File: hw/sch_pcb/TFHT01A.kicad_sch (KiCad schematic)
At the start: 13 parts, among them J2 SM04B-GHS-TB, M2 M3, U3 MIC5504-3.3YM5

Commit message: Update schematics title block.
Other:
- title: TFI2CEXT01A -> TFHT01A
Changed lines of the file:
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@@
   (paper "A4")
   (title_block
-    (title "TFI2CEXT01A")
-    (date "2021-01-23")
+    (title "TFHT01A")
+    (date "2021-04-05")
     (company "ThunderFly s.r.o.")
-    (comment 1 "I2C expander")
+    (comment 1 "Humidity and Temperature \\n sensor \\n ")
     (comment 2 "Jacho  <info@thunderfly.cz>")
   )

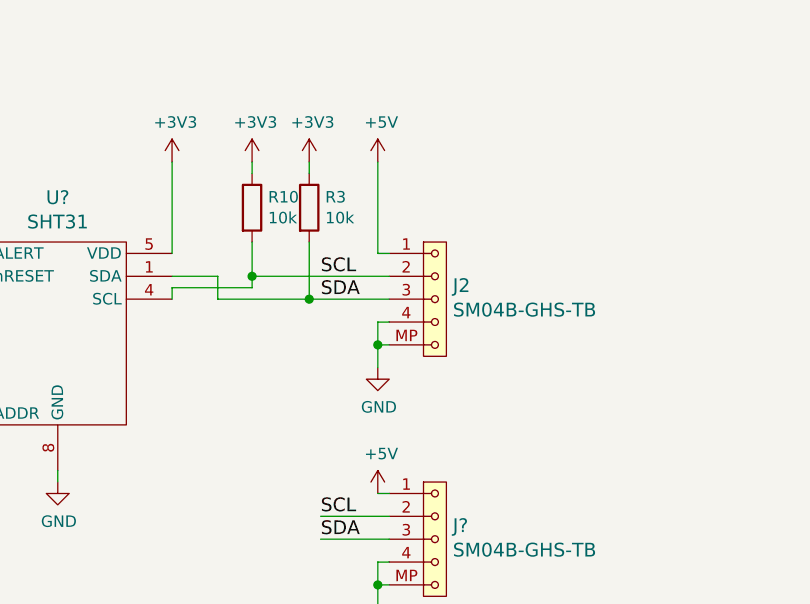
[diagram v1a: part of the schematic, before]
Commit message: Schematic traces cleanup.
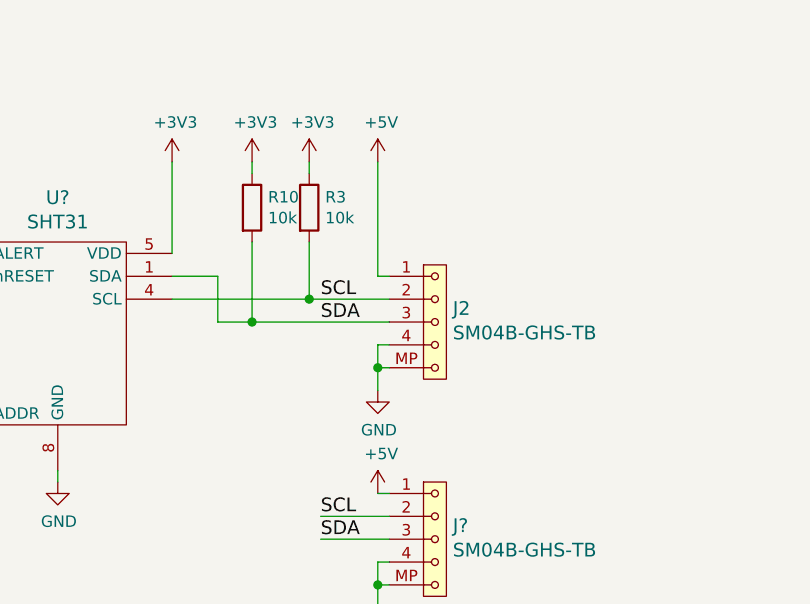
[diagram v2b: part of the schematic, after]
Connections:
- net SCL: now also R3.2; no longer R10.2
- net SDA: now also R10.2; no longer R3.2
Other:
- moved on the sheet: J2
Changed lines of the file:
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@@
   (junction (at 81.28 168.91) (diameter 1.016) (color 0 0 0 0))
   (junction (at 111.76 92.71) (diameter 1.016) (color 0 0 0 0))
-  (junction (at 147.32 95.25) (diameter 1.016) (color 0 0 0 0))
+  (junction (at 147.32 100.33) (diameter 1.016) (color 0 0 0 0))
   (junction (at 153.67 97.79) (diameter 1.016) (color 0 0 0 0))
-  (junction (at 161.29 102.87) (diameter 1.016) (color 0 0 0 0))
+  (junction (at 161.29 105.41) (diameter 1.016) (color 0 0 0 0))
   (junction (at 161.29 129.54) (diameter 1.016) (color 0 0 0 0))
   (wire (pts (xy 27.94 167.64) (xy 27.94 168.91))
@@
     (stroke (width 0) (type solid) (color 0 0 0 0))
   )
-  (wire (pts (xy 138.43 96.52) (xy 138.43 97.79))
-    (stroke (width 0) (type solid) (color 0 0 0 0))
-  )
-  (wire (pts (xy 143.51 95.25) (xy 143.51 97.79))
-    (stroke (width 0) (type solid) (color 0 0 0 0))
-  )
-  (wire (pts (xy 143.51 97.79) (xy 153.67 97.79))
+  (wire (pts (xy 138.43 97.79) (xy 153.67 97.79))
+    (stroke (width 0) (type solid) (color 0 0 0 0))
+  )
+  (wire (pts (xy 143.51 95.25) (xy 143.51 100.33))
+    (stroke (width 0) (type solid) (color 0 0 0 0))
+  )
+  (wire (pts (xy 143.51 100.33) (xy 147.32 100.33))
     (stroke (width 0) (type solid) (color 0 0 0 0))
   )
@@
     (stroke (width 0) (type solid) (color 0 0 0 0))
   )
-  (wire (pts (xy 147.32 91.44) (xy 147.32 95.25))
-    (stroke (width 0) (type solid) (color 0 0 0 0))
-  )
-  (wire (pts (xy 147.32 95.25) (xy 147.32 96.52))
-    (stroke (width 0) (type solid) (color 0 0 0 0))
-  )
-  (wire (pts (xy 147.32 95.25) (xy 162.56 95.25))
-    (stroke (width 0) (type solid) (color 0 0 0 0))
-  )
-  (wire (pts (xy 147.32 96.52) (xy 138.43 96.52))
+  (wire (pts (xy 147.32 91.44) (xy 147.32 100.33))
+    (stroke (width 0) (type solid) (color 0 0 0 0))
+  )
+  (wire (pts (xy 147.32 100.33) (xy 162.56 100.33))
     (stroke (width 0) (type solid) (color 0 0 0 0))
   )
@@
     (stroke (width 0) (type solid) (color 0 0 0 0))
   )
-  (wire (pts (xy 161.29 82.55) (xy 161.29 92.71))
-    (stroke (width 0) (type solid) (color 0 0 0 0))
-  )
-  (wire (pts (xy 161.29 92.71) (xy 162.56 92.71))
-    (stroke (width 0) (type solid) (color 0 0 0 0))
-  )
-  (wire (pts (xy 161.29 100.33) (xy 161.29 102.87))
+  (wire (pts (xy 161.29 82.55) (xy 161.29 95.25))
+    (stroke (width 0) (type solid) (color 0 0 0 0))
+  )
+  (wire (pts (xy 161.29 95.25) (xy 162.56 95.25))
     (stroke (width 0) (type solid) (color 0 0 0 0))
   )
@@
     (stroke (width 0) (type solid) (color 0 0 0 0))
   )
+  (wire (pts (xy 161.29 105.41) (xy 161.29 107.95))
+    (stroke (width 0) (type solid) (color 0 0 0 0))
+  )
   (wire (pts (xy 161.29 119.38) (xy 162.56 119.38))
     (stroke (width 0) (type solid) (color 0 0 0 0))
@@
     (stroke (width 0) (type solid) (color 0 0 0 0))
   )
-  (wire (pts (xy 162.56 100.33) (xy 161.29 100.33))
-    (stroke (width 0) (type solid) (color 0 0 0 0))
-  )
   (wire (pts (xy 162.56 102.87) (xy 161.29 102.87))
+    (stroke (width 0) (type solid) (color 0 0 0 0))
+  )
+  (wire (pts (xy 162.56 105.41) (xy 161.29 105.41))
     (stroke (width 0) (type solid) (color 0 0 0 0))
   )
@@
     (effects (font (size 1.524 1.524)) (justify left bottom))
   )
-  (label "SCL" (at 154.94 95.25 0)
+  (label "SCL" (at 154.94 97.79 0)
     (effects (font (size 1.524 1.524)) (justify left bottom))
   )
-  (label "SDA" (at 154.94 97.79 0)
+  (label "SDA" (at 154.94 100.33 0)
     (effects (font (size 1.524 1.524)) (justify left bottom))
   )
@@
     (pin "1")
   )
-  (symbol (lib_id "power:GND") (at 161.29 105.41 0) (unit 1)
-    (in_bom yes) (on_board yes)
-    (property "Reference" "#PWR09" (id 0) (at 161.29 111.76 0)
-      (effects (font (size 1.27 1.27)) hide)
-    )
-    (property "Value" "GND" (id 1) (at 161.417 109.8042 0))
-    (property "Footprint" "" (id 2) (at 161.29 105.41 0)
-      (effects (font (size 1.27 1.27)) hide)
-    )
-    (property "Datasheet" "" (id 3) (at 161.29 105.41 0)
+  (symbol (lib_id "power:GND") (at 161.29 107.95 0) (unit 1)
+    (in_bom yes) (on_board yes)
+    (property "Reference" "#PWR09" (id 0) (at 161.29 114.3 0)
+      (effects (font (size 1.27 1.27)) hide)
+    )
+    (property "Value" "GND" (id 1) (at 161.417 112.3442 0))
+    (property "Footprint" "" (id 2) (at 161.29 107.95 0)
+      (effects (font (size 1.27 1.27)) hide)
+    )
+    (property "Datasheet" "" (id 3) (at 161.29 107.95 0)
       (effects (font (size 1.27 1.27)) hide)
     )
@@
     (pin "3")
   )
-  (symbol (lib_id "MLAB_CONNECTORS_JST:SM04B-GHS-TB") (at 167.64 97.79 0) (unit 1)
-    (in_bom yes) (on_board yes)
-    (property "Reference" "J2" (id 0) (at 169.6212 96.2914 0)
+  (symbol (lib_id "MLAB_CONNECTORS_JST:SM04B-GHS-TB") (at 167.64 100.33 0) (unit 1)
+    (in_bom yes) (on_board yes)
+    (property "Reference" "J2" (id 0) (at 169.6212 98.8314 0)
       (effects (font (size 1.524 1.524)) (justify left))
     )
-    (property "Value" "SM04B-GHS-TB" (id 1) (at 169.6212 99.0092 0)
+    (property "Value" "SM04B-GHS-TB" (id 1) (at 169.6212 101.5492 0)
       (effects (font (size 1.524 1.524)) (justify left))
     )
-    (property "Footprint" "Connector_JST:JST_GH_SM04B-GHS-TB_1x04-1MP_P1.25mm_Horizontal" (id 2) (at 167.64 92.71 0)
-      (effects (font (size 1.524 1.524)) hide)
-    )
-    (property "Datasheet" "" (id 3) (at 167.64 92.71 0)
-      (effects (font (size 1.524 1.524)))
-    )
-    (property "UST_id" "" (id 4) (at 167.64 97.79 0)
-      (effects (font (size 1.27 1.27)) hide)
-    )
-    (property "UST_ID" "5c86273d1287500b4e0280be" (id 5) (at 167.64 97.79 0)
-      (effects (font (size 1.27 1.27)) hide)
-    )
+    (property "Footprint" "Connector_JST:JST_GH_SM04B-GHS-TB_1x04-1MP_P1.25mm_Horizontal" (id 2) (at 167.64 95.25 0)
+      (effects (font (size 1.524 1.524)) hide)
+    )
+    (property "Datasheet" "" (id 3) (at 167.64 95.25 0)
+      (effects (font (size 1.524 1.524)))
+    )
+    (property "UST_id" "" (id 4) (at 167.64 100.33 0)
+      (effects (font (size 1.27 1.27)) hide)
+    )
+    (property "UST_ID" "5c86273d1287500b4e0280be" (id 5) (at 167.64 100.33 0)
+      (effects (font (size 1.27 1.27)) hide)
+    )

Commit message: Edit PCB
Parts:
- added D2: LED GREEN, Mlab_D:LED_1206, symbol Device:LED
- added D3: LED RED, Mlab_D:LED_1206, symbol Device:LED
- added M1, M3, M4, M5, M6: M3, Mlab_Mechanical:dira_3mm, symbol MLAB_MECHANICAL:HOLE
- added Q1: BC817, Package_TO_SOT_SMD:SOT-23, symbol Transistor_BJT:BC817
- added R1, R4: 180R, Mlab_R:SMD-0603, symbol Device:R
- added R2: 100R, Mlab_R:SMD-0603, symbol Device:R
- D1: value ZENER-6.2V -> BZX585-B5V6.115; footprint Mlab_D:Diode-MiniMELF_Standard -> Diode_SMD:D_SOD-523
- M2: footprint Mlab_Mechanical:MountingHole_3mm -> Mlab_Mechanical:dira_3mm
- U1: renamed from U?; footprint (none) -> Mlab_IO:DFN-8-1EP_2.4x2.4mm_Pitch0.5mm
- gave numbers to parts that had none: 2
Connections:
- net +3V3: no longer U1.3 (ALERT), U1.6 (nRESET)
- net +5V: now also D3.2 (A), R1.1
- net GND: now also D2.1 (K), Q1.2 (E); no longer M2.1
- new net: Q1.1 (B), R2.2
- new net: Q1.3 (C), R4.2
- new net: D3.1 (K), R4.1
- new net: D2.2 (A), R1.2
- new net ALERT: R2.1, U1.3 (ALERT)
- no-connect marks 0 -> 7
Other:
- note removed: "BZX585-B5V6.115 NEXPERIA"

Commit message: Minor graphics improvement.
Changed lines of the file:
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@@
     (stroke (width 0) (type solid) (color 0 0 0 0))
   )
-  (polyline (pts (xy 236.22 27.94) (xy 236.22 17.78))
+  (polyline (pts (xy 236.22 17.78) (xy 280.67 17.78))
     (stroke (width 0) (type dash) (color 0 0 0 0))
   )
-  (polyline (pts (xy 255.27 17.78) (xy 280.67 17.78))
+  (polyline (pts (xy 236.22 27.94) (xy 236.22 17.78))
     (stroke (width 0) (type dash) (color 0 0 0 0))
   )
@@
     (stroke (width 0) (type dash) (color 0 0 0 0))
   )
-  (polyline (pts (xy 280.67 27.94) (xy 255.27 27.94))
+  (polyline (pts (xy 280.67 27.94) (xy 236.22 27.94))
     (stroke (width 0) (type dash) (color 0 0 0 0))
   )

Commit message: Edit
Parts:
- D1: UST_ID 604b0326128750769e5b0f93 -> 60879d38128750769ee58e48
- D2: UST_ID (none) -> 5c70984412875079b91f8895
- D3: UST_ID (none) -> 5c70984412875079b91f8896
- Q1: UST_ID (none) -> 5c70984712875079b91f8aec
- R1, R4: UST_ID (none) -> 5c70984512875079b91f8957
- R10, R3: UST_ID 5c70984612875079b91f899f -> 5c70984512875079b91f8962
- R2: UST_ID (none) -> 5c70984512875079b91f8956
- U1: UST_ID (none) -> 5c70984612875079b91f89e4
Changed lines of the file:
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@@
+      (effects (font (size 1.27 1.27)) hide)
+    )
+    (property "UST_ID" "5c70984512875079b91f8957" (id 4) (at 20.32 168.91 0)
       (effects (font (size 1.27 1.27)) hide)
     )
@@
       (effects (font (size 1.27 1.27)) hide)
     )
-    (property "UST_ID" "5c70984612875079b91f899f" (id 5) (at 147.32 87.63 0)
+    (property "UST_ID" "5c70984512875079b91f8962" (id 5) (at 147.32 87.63 0)
       (effects (font (size 1.27 1.27)) hide)
     )
@@
       (effects (font (size 1.27 1.27)) hide)
     )
-    (property "UST_ID" "5c70984612875079b91f899f" (id 5) (at 153.67 87.63 0)
+    (property "UST_ID" "5c70984512875079b91f8962" (id 5) (at 153.67 87.63 0)
       (effects (font (size 1.27 1.27)) hide)
     )
@@
       (effects (font (size 1.27 1.27)) hide)
     )
+    (property "UST_ID" "5c70984512875079b91f8956" (id 4) (at 255.27 144.78 0)
+      (effects (font (size 1.27 1.27)) hide)
+    )
     (pin "1")
     (pin "2")
@@
       (effects (font (size 1.27 1.27)) hide)
     )
+    (property "UST_ID" "5c70984512875079b91f8957" (id 4) (at 269.24 133.35 0)
+      (effects (font (size 1.27 1.27)) hide)
+    )
     (pin "1")
     (pin "2")
@@
       (effects (font (size 1.27 1.27)) hide)
     )
-    (property "UST_ID" "604b0326128750769e5b0f93" (id 5) (at 43.18 175.26 0)
+    (property "UST_ID" "60879d38128750769ee58e48" (id 5) (at 43.18 175.26 0)
       (effects (font (size 1.27 1.27)) hide)
     )
@@
       (effects (font (size 1.27 1.27)) hide)
     )
+    (property "UST_ID" "5c70984412875079b91f8895" (id 4) (at 20.32 177.8 0)
+      (effects (font (size 1.27 1.27)) hide)
+    )
     (pin "1")
     (pin "2")
@@
     )
     (property "Datasheet" "~" (id 3) (at 269.24 123.19 0)
+      (effects (font (size 1.27 1.27)) hide)
+    )
+    (property "UST_ID" "5c70984412875079b91f8896" (id 4) (at 269.24 123.19 0)
       (effects (font (size 1.27 1.27)) hide)
     )
@@
       (effects (font (size 1.27 1.27)) (justify left) hide)
     )
+    (property "UST_ID" "5c70984712875079b91f8aec" (id 4) (at 266.7 144.78 0)
+      (effects (font (size 1.27 1.27)) hide)
+    )
     (pin "1")
     (pin "2")
@@
       (effects (font (size 1.524 1.524)))
     )
-    (pin "1")
+    (property "UST_ID" "5c70984612875079b91f89e4" (id 4) (at 127 102.87 0)
+      (effects (font (size 1.27 1.27)) hide)
+    )
+    (pin "1")
